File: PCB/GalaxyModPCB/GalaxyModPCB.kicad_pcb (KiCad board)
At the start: 2 copper layers, 63.5 x 38.2 mm, 66 parts, among them J1 LED RGBW Connector, J2 USB to UART, J3 Motor Connector, J4 Projector Connector, J5 Debug Header, J6 Power Header, J7 Boot mode, Q1 IRLML0030, Q2 IRLML0030, Q3 IRLML0030, Q4 IRLML0030, Q5 IRLML0030, Q6 IRLML0030, SW1 On/Off, SW2 Colour, SW3 Brightness, SW4 Motor, U1 ESP32-WROOM-32, U2 AMS1117-3.3

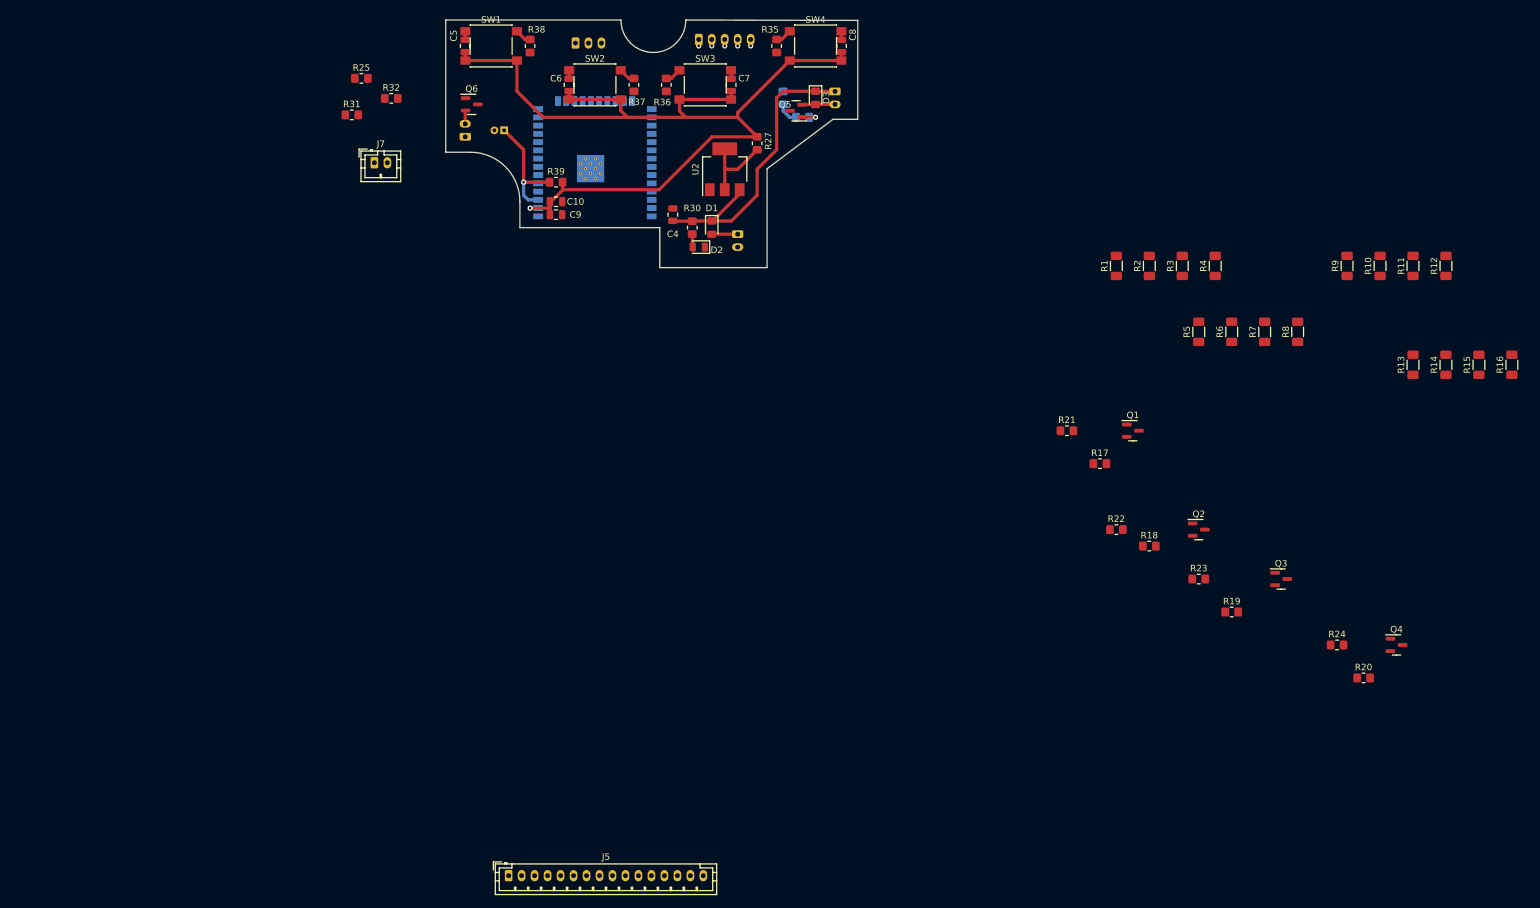
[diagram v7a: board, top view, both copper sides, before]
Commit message: Corrected component sides
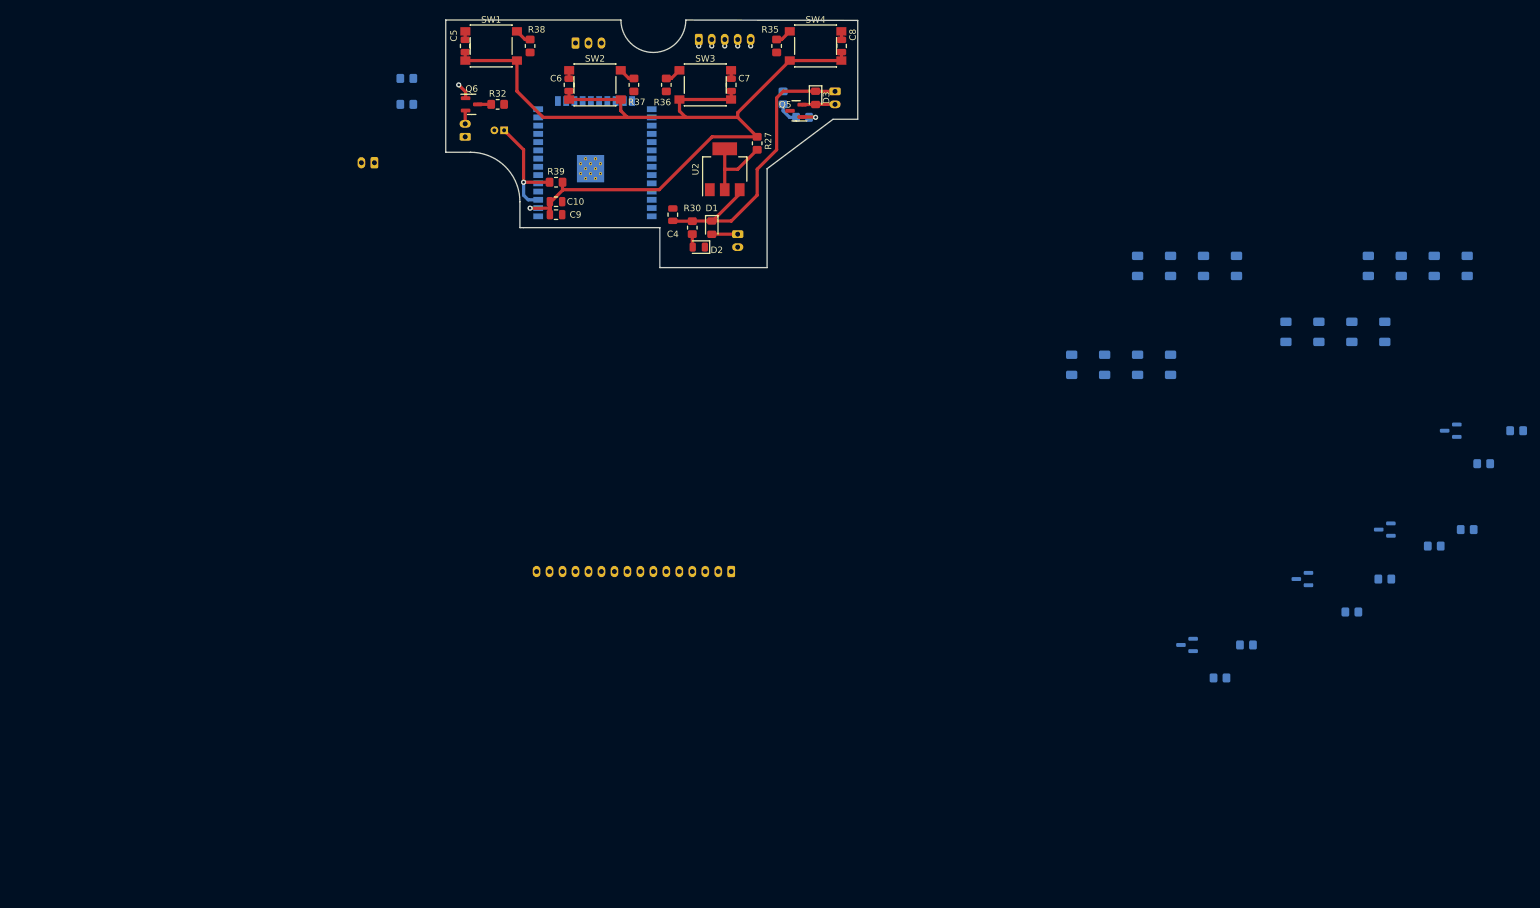
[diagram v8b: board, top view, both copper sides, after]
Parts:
- J5, J7, Q1, Q2, Q3, Q4, R1, R10, R11, R12, R13, R14, R15, R16, R17, R18, R19, R2, R20, R21, R22, R23, R24, R25, R3, R31, R4, R5, R6, R7, R8, R9: moved to B.Cu
- moved R21 69.3 mm to (275.1, 114.3), turned to 180 degrees
- moved R16 67.8 mm to (206.5, 104.1)
- moved R17 59.2 mm to (270.0, 119.4), turned to 180 degrees
- moved J5 58.1 mm to (154.0, 136.0), turned to 180 degrees
- moved R15 57.7 mm to (211.6, 104.1)
- moved R1 54.1 mm to (267.4, 88.9)
- moved R22 54.1 mm to (267.4, 129.5), turned to 180 degrees
- moved Q1 49.0 mm to (264.9, 114.3), turned to 180 degrees
- moved R12 47.5 mm to (216.6, 88.9)
- moved R14 47.5 mm to (216.6, 104.1)
- moved R18 43.9 mm to (262.4, 132.1), turned to 180 degrees
- moved R2 43.9 mm to (262.4, 88.9)
- moved R11 37.4 mm to (221.7, 88.9)
- moved R13 37.4 mm to (221.7, 104.1)
- moved R3 33.8 mm to (257.3, 88.9)
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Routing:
- net Net-(Q6-Pad1): track 0.00 -> 2.49 mm, vias 0 -> 1
- net GNDREF: track 0.00 -> 2.06 mm
